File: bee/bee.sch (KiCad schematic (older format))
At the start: 12 parts, among them J1 Conn_01x02_Male, J2 Conn_01x02_Male, J3 Conn_01x02_Male, J4 Conn_01x02_Male

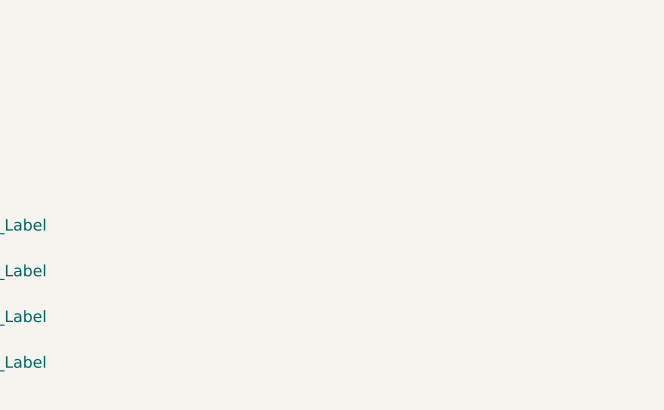
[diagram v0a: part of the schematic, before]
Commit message: Replace vias by mounting holes.
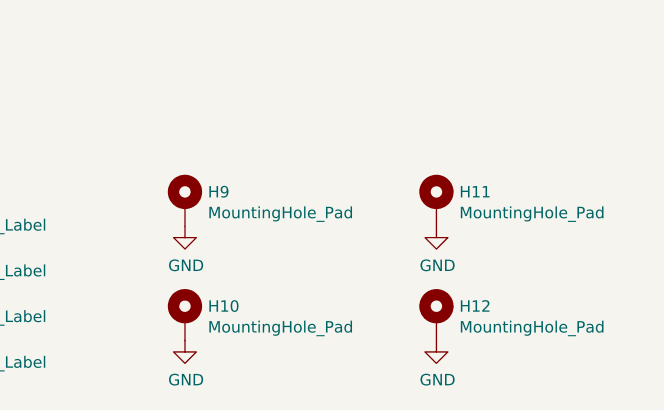
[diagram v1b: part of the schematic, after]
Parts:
- added H10, H11, H12, H9: MountingHole_Pad, MountingHole:MountingHole_3.2mm_M3_ISO7380_Pad, symbol Mechanical:MountingHole_Pad
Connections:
- net GND: now also H10.1, H11.1, H12.1, H9.1
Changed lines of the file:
@@
+	1    0    0    -1
+$EndComp
+$Comp
+L Mechanical:MountingHole_Pad H10
+U 1 1 5CC7D33F
+P 3000 7400
+F 0 "H10" H 3100 7449 50  0000 L CNN
+F 1 "MountingHole_Pad" H 3100 7358 50  0000 L CNN
+F 2 "MountingHole:MountingHole_3.2mm_M3_ISO7380_Pad" H 3000 7400 50  0001 C CNN
+F 3 "~" H 3000 7400 50  0001 C CNN
+	1    3000 7400
+	1    0    0    -1
+$EndComp
+$Comp
+L power:GND #PWR0101
+U 1 1 5CC7D8D3
+P 3000 7500
+F 0 "#PWR0101" H 3000 7250 50  0001 C CNN
+F 1 "GND" H 3005 7327 50  0000 C CNN
+F 2 "" H 3000 7500 50  0001 C CNN
+F 3 "" H 3000 7500 50  0001 C CNN
+	1    3000 7500
+	1    0    0    -1
+$EndComp
+$Comp
+L Mechanical:MountingHole_Pad H12
+U 1 1 5CC7EE06
+P 4100 7400
+F 0 "H12" H 4200 7449 50  0000 L CNN
+F 1 "MountingHole_Pad" H 4200 7358 50  0000 L CNN
+F 2 "MountingHole:MountingHole_3.2mm_M3_ISO7380_Pad" H 4100 7400 50  0001 C CNN
+F 3 "~" H 4100 7400 50  0001 C CNN
+	1    4100 7400
+	1    0    0    -1
+$EndComp
+$Comp
+L power:GND #PWR0102
+U 1 1 5CC7EE10
+P 4100 7500
+F 0 "#PWR0102" H 4100 7250 50  0001 C CNN
+F 1 "GND" H 4105 7327 50  0000 C CNN
+F 2 "" H 4100 7500 50  0001 C CNN
+F 3 "" H 4100 7500 50  0001 C CNN
+	1    4100 7500
+	1    0    0    -1
+$EndComp
+$Comp
+L Mechanical:MountingHole_Pad H9
+U 1 1 5CC7FAE4
+P 3000 6900
+F 0 "H9" H 3100 6949 50  0000 L CNN
+F 1 "MountingHole_Pad" H 3100 6858 50  0000 L CNN
+F 2 "MountingHole:MountingHole_3.2mm_M3_ISO7380_Pad" H 3000 6900 50  0001 C CNN
+F 3 "~" H 3000 6900 50  0001 C CNN
+	1    3000 6900
+	1    0    0    -1
+$EndComp
+$Comp
+L power:GND #PWR0103
+U 1 1 5CC7FAEE
+P 3000 7000
+F 0 "#PWR0103" H 3000 6750 50  0001 C CNN
+F 1 "GND" H 3005 6827 50  0000 C CNN
+F 2 "" H 3000 7000 50  0001 C CNN
+F 3 "" H 3000 7000 50  0001 C CNN
+	1    3000 7000
+	1    0    0    -1
+$EndComp
+$Comp
+L Mechanical:MountingHole_Pad H11
+U 1 1 5CC7FAF8
+P 4100 6900
+F 0 "H11" H 4200 6949 50  0000 L CNN
+F 1 "MountingHole_Pad" H 4200 6858 50  0000 L CNN
+F 2 "MountingHole:MountingHole_3.2mm_M3_ISO7380_Pad" H 4100 6900 50  0001 C CNN
+F 3 "~" H 4100 6900 50  0001 C CNN
+	1    4100 6900
+	1    0    0    -1
+$EndComp
+$Comp
+L power:GND #PWR0104
+U 1 1 5CC7FB02
+P 4100 7000
+F 0 "#PWR0104" H 4100 6750 50  0001 C CNN
+F 1 "GND" H 4105 6827 50  0000 C CNN
+F 2 "" H 4100 7000 50  0001 C CNN
+F 3 "" H 4100 7000 50  0001 C CNN
+	1    4100 7000
 	1    0    0    -1
 $EndComp

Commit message: Add part numbers.
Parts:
- J1, J2, J3, J4: Reichelt Part No (none) -> RND 205-00623
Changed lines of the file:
@@
 EESchema Schematic File Version 4
 LIBS:bee-cache
-EELAYER 29 0
+EELAYER 26 0
 EELAYER END
 $Descr A4 11693 8268
@@
 F 2 "Connector_PinHeader_2.54mm:PinHeader_1x02_P2.54mm_Vertical" H 850 1300 50  0001 C CNN
 F 3 "~" H 850 1300 50  0001 C CNN
+F 4 "RND 205-00623" H 850 1300 50  0001 C CNN "Reichelt Part No"
 	1    850  1300
 	1    0    0    -1
@@
 F 2 "Connector_PinHeader_2.54mm:PinHeader_1x02_P2.54mm_Vertical" H 850 950 50  0001 C CNN
 F 3 "~" H 850 950 50  0001 C CNN
+F 4 "RND 205-00623" H 850 950 50  0001 C CNN "Reichelt Part No"
 	1    850  950
 	1    0    0    -1
@@
 F 2 "Connector_PinHeader_2.54mm:PinHeader_1x02_P2.54mm_Vertical" H 850 2150 50  0001 C CNN
 F 3 "~" H 850 2150 50  0001 C CNN
+F 4 "RND 205-00623" H 850 2150 50  0001 C CNN "Reichelt Part No"
 	1    850  2150
 	1    0    0    -1
@@
 F 2 "Connector_PinHeader_2.54mm:PinHeader_1x02_P2.54mm_Vertical" H 850 1800 50  0001 C CNN
 F 3 "~" H 850 1800 50  0001 C CNN
+F 4 "RND 205-00623" H 850 1800 50  0001 C CNN "Reichelt Part No"
 	1    850  1800
 	1    0    0    -1

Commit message: Relabel as bee specific.
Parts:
- H1, H2: footprint Symbol-emt:Text_U_B+_Silkscreen -> Symbol-bee:Text_U_B+_Silkscreen; symbol Mechanical-emt:Silkscreen_Label -> Mechanical-bee:Silkscreen_Label
- H3, H4: footprint Symbol-emt:Text_U_B-_Silkscreen -> Symbol-bee:Text_U_B-_Silkscreen; symbol Mechanical-emt:Silkscreen_Label -> Mechanical-bee:Silkscreen_Label
- H5, H6: footprint Symbol-emt:Text_U_B2_Silkscreen -> Symbol-bee:Text_U_B2_Silkscreen; symbol Mechanical-emt:Silkscreen_Label -> Mechanical-bee:Silkscreen_Label
- H7, H8: footprint Symbol-emt:Symbol_GND_Silkscreen -> Symbol-bee:Symbol_GND_Silkscreen; symbol Mechanical-emt:Silkscreen_Label -> Mechanical-bee:Silkscreen_Label
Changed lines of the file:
@@
 	1050 1400 1450 1400
 $Comp
-L Mechanical-emt:Silkscreen_Label H4
+L Mechanical-bee:Silkscreen_Label H4
 U 1 1 5CC7107F
 P 800 7550
 F 0 "H4" H 925 7595 50  0000 L CNN
 F 1 "Silkscreen_Label" H 925 7504 50  0000 L CNN
-F 2 "Symbol-emt:Text_U_B-_Silkscreen" H 800 7550 50  0001 C CNN
+F 2 "Symbol-bee:Text_U_B-_Silkscreen" H 800 7550 50  0001 C CNN
 F 3 "~" H 800 7550 50  0001 C CNN
 	1    800  7550
@@
 $EndComp
 $Comp
-L Mechanical-emt:Silkscreen_Label H3
+L Mechanical-bee:Silkscreen_Label H3
 U 1 1 5CC72C74
 P 800 7350
 F 0 "H3" H 925 7395 50  0000 L CNN
 F 1 "Silkscreen_Label" H 925 7304 50  0000 L CNN
-F 2 "Symbol-emt:Text_U_B-_Silkscreen" H 800 7350 50  0001 C CNN
+F 2 "Symbol-bee:Text_U_B-_Silkscreen" H 800 7350 50  0001 C CNN
 F 3 "~" H 800 7350 50  0001 C CNN
 	1    800  7350
@@
 $EndComp
 $Comp
-L Mechanical-emt:Silkscreen_Label H2
+L Mechanical-bee:Silkscreen_Label H2
 U 1 1 5CC72FEF
 P 800 7150
 F 0 "H2" H 925 7195 50  0000 L CNN
 F 1 "Silkscreen_Label" H 925 7104 50  0000 L CNN
-F 2 "Symbol-emt:Text_U_B+_Silkscreen" H 800 7150 50  0001 C CNN
+F 2 "Symbol-bee:Text_U_B+_Silkscreen" H 800 7150 50  0001 C CNN
 F 3 "~" H 800 7150 50  0001 C CNN
 	1    800  7150
@@
 $EndComp
 $Comp
-L Mechanical-emt:Silkscreen_Label H1
+L Mechanical-bee:Silkscreen_Label H1
 U 1 1 5CC7323E
 P 800 6950
 F 0 "H1" H 925 6995 50  0000 L CNN
 F 1 "Silkscreen_Label" H 925 6904 50  0000 L CNN
-F 2 "Symbol-emt:Text_U_B+_Silkscreen" H 800 6950 50  0001 C CNN
+F 2 "Symbol-bee:Text_U_B+_Silkscreen" H 800 6950 50  0001 C CNN
 F 3 "~" H 800 6950 50  0001 C CNN
 	1    800  6950
@@
 $EndComp
 $Comp
-L Mechanical-emt:Silkscreen_Label H5
+L Mechanical-bee:Silkscreen_Label H5
 U 1 1 5CC7350D
 P 1700 6950
 F 0 "H5" H 1825 6995 50  0000 L CNN
 F 1 "Silkscreen_Label" H 1825 6904 50  0000 L CNN
-F 2 "Symbol-emt:Text_U_B2_Silkscreen" H 1700 6950 50  0001 C CNN
+F 2 "Symbol-bee:Text_U_B2_Silkscreen" H 1700 6950 50  0001 C CNN
 F 3 "~" H 1700 6950 50  0001 C CNN
 	1    1700 6950
@@
 $EndComp
 $Comp
-L Mechanical-emt:Silkscreen_Label H6
+L Mechanical-bee:Silkscreen_Label H6
 U 1 1 5CC73D6A
 P 1700 7150
 F 0 "H6" H 1825 7195 50  0000 L CNN
 F 1 "Silkscreen_Label" H 1825 7104 50  0000 L CNN
-F 2 "Symbol-emt:Text_U_B2_Silkscreen" H 1700 7150 50  0001 C CNN
+F 2 "Symbol-bee:Text_U_B2_Silkscreen" H 1700 7150 50  0001 C CNN
 F 3 "~" H 1700 7150 50  0001 C CNN
 	1    1700 7150
@@
 $EndComp
 $Comp
-L Mechanical-emt:Silkscreen_Label H7
+L Mechanical-bee:Silkscreen_Label H7
 U 1 1 5CC740AE
 P 1700 7350
 F 0 "H7" H 1825 7395 50  0000 L CNN
 F 1 "Silkscreen_Label" H 1825 7304 50  0000 L CNN
-F 2 "Symbol-emt:Symbol_GND_Silkscreen" H 1700 7350 50  0001 C CNN
+F 2 "Symbol-bee:Symbol_GND_Silkscreen" H 1700 7350 50  0001 C CNN
 F 3 "~" H 1700 7350 50  0001 C CNN
 	1    1700 7350
@@
 $EndComp
 $Comp
-L Mechanical-emt:Silkscreen_Label H8
+L Mechanical-bee:Silkscreen_Label H8
 U 1 1 5CC742F3
 P 1700 7550
 F 0 "H8" H 1825 7595 50  0000 L CNN
 F 1 "Silkscreen_Label" H 1825 7504 50  0000 L CNN
-F 2 "Symbol-emt:Symbol_GND_Silkscreen" H 1700 7550 50  0001 C CNN
+F 2 "Symbol-bee:Symbol_GND_Silkscreen" H 1700 7550 50  0001 C CNN
 F 3 "~" H 1700 7550 50  0001 C CNN
 	1    1700 7550
